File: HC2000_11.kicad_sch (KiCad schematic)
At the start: 16 parts

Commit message: Updated ICs values and positions
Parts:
- UA8, UC8: value 2k x 4bit -> 2k x 4bit/-
- UE8A0: value 27128P -> 27128P/-
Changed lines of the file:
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@@
       (effects (font (size 1.778 1.5113)) (justify left bottom))
     )
-    (property "Value" "2k x 4bit" (at 148.59 177.8 0)
+    (property "Value" "2k x 4bit/-" (at 148.59 177.8 0)
       (effects (font (size 1.778 1.5113)) (justify left bottom))
     )
@@
       (effects (font (size 1.778 1.5113)) (justify left bottom))
     )
-    (property "Value" "27128P" (at 107.95 167.64 0)
+    (property "Value" "27128P/-" (at 107.95 167.64 0)
       (effects (font (size 1.778 1.5113)) (justify left bottom))
     )
@@
       (effects (font (size 1.778 1.5113)) (justify left bottom))
     )
-    (property "Value" "2k x 4bit" (at 189.23 177.8 0)
-      (effects (font (size 1.778 1.5113)) (justify left bottom))
-    )
+    (property "Value" "2k x 4bit/-" (at 189.23 177.8 0)
+      (effects (font (size 1.778 1.5113)) (justify left bottom))
+    )

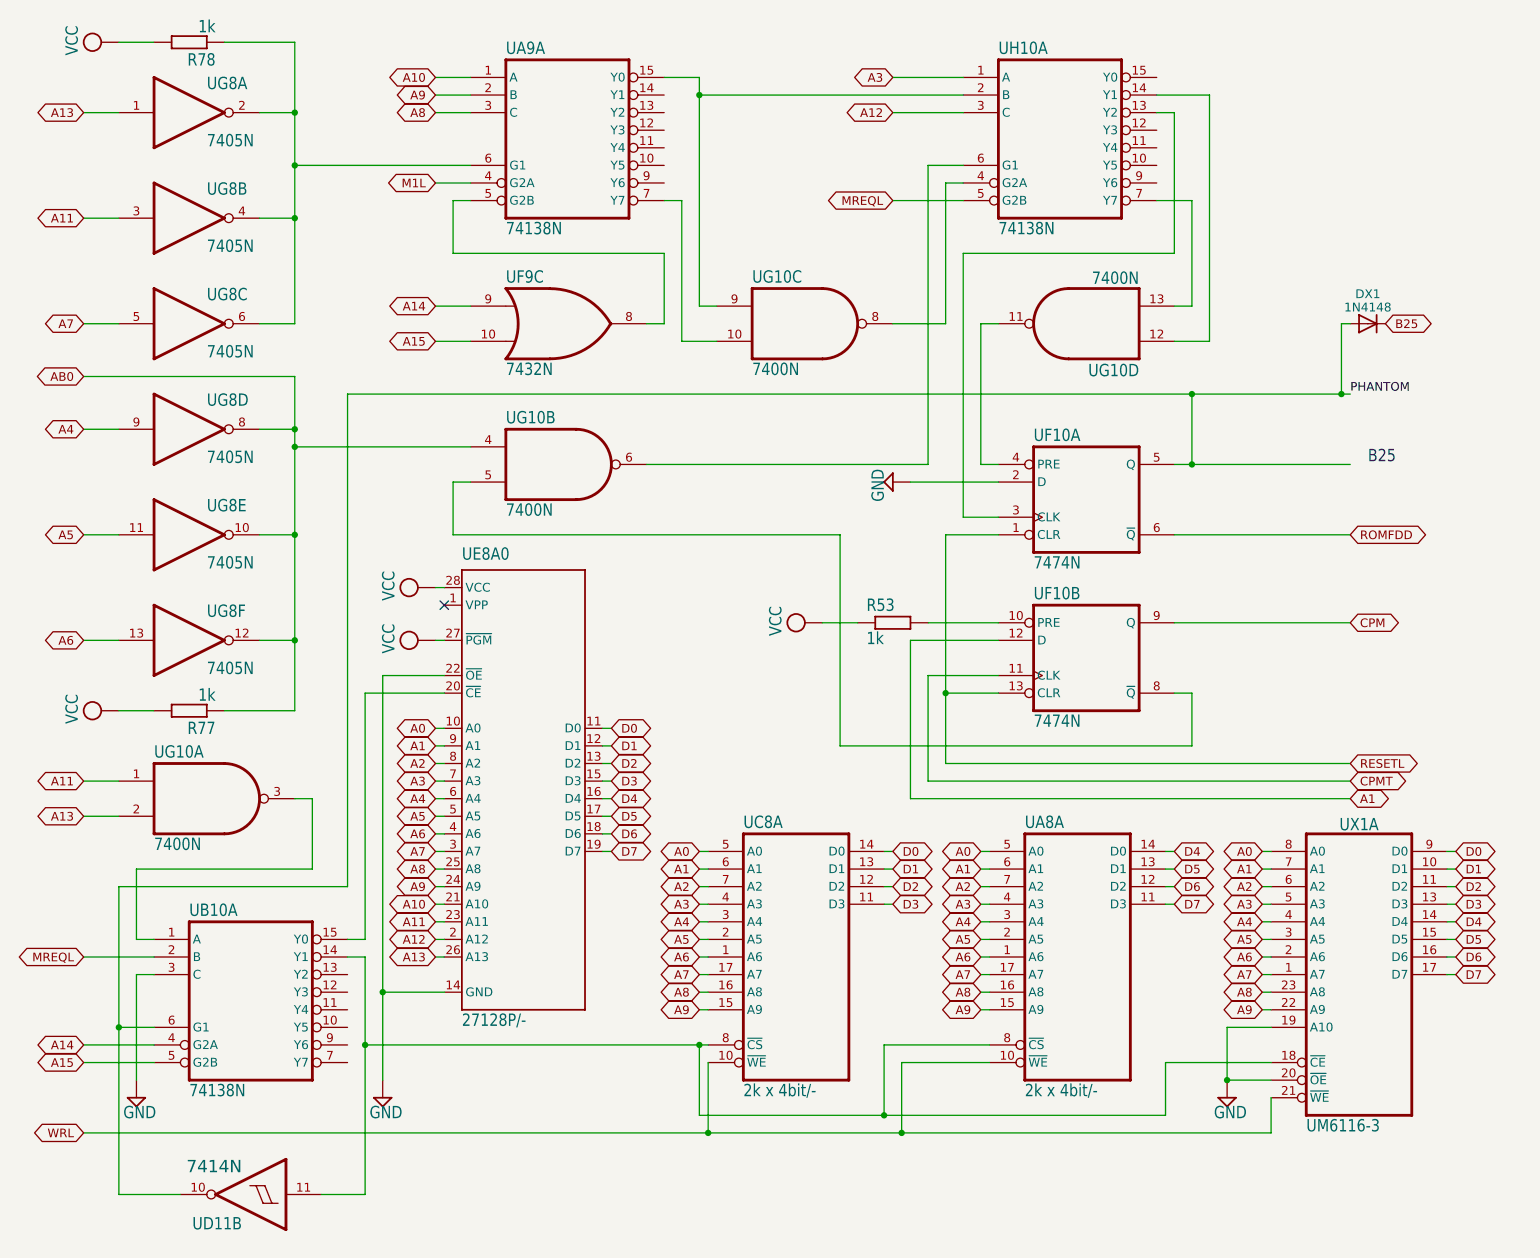
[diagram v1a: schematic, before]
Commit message: Fix errors (IC & unnoticed cut for 1 EPROM)
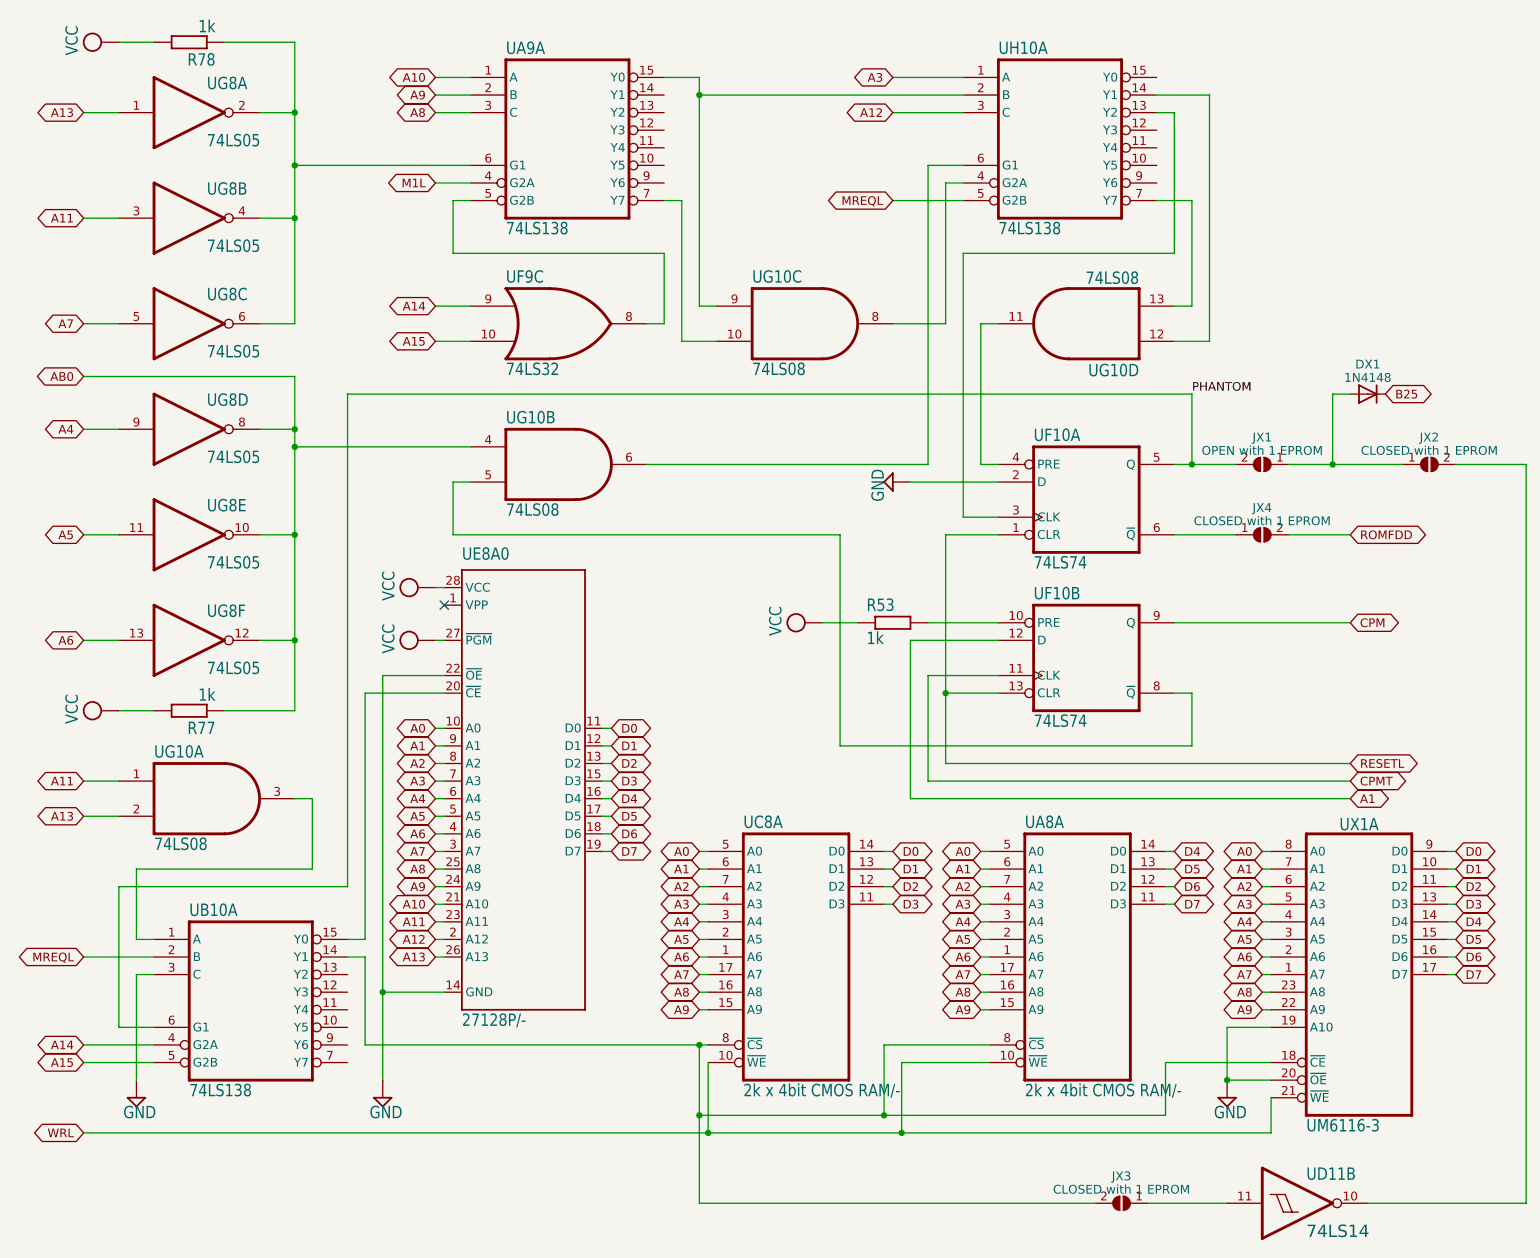
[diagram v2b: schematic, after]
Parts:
- added JX1: OPEN with 1 EPROM, HC2000:SolderJumper-2_P1.3mm_Open_Pad1.0x1.5mm, symbol HC2000:SolderJumper_2_Open
- added JX2, JX3, JX4: CLOSED with 1 EPROM, HC2000:SolderJumper-2_P1.3mm_Open_Pad1.0x1.5mm, symbol HC2000:SolderJumper_2_Open
- UA8, UC8: value 2k x 4bit/- -> 2k x 4bit CMOS RAM/-
- UA9, UB10, UH10: value 74138N -> 74LS138
- UD11: value 7414N -> 74LS14
- UF10: value 7474N -> 74LS74
- UF9: value 7432N -> 74LS32
- UG10: value 7400N -> 74LS08; symbol HC2000:7400N -> HC2000:7408N
- UG8: value 7405N -> 74LS05
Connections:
- net PHANTOM: now also JX1.2 (B); no longer DX1.A, UD11.10 (O)
- net ROMFDD: now also JX4.2 (B); no longer UF10.6 (~{Q})
- net at UA8.8 (~{CS}), UB10.14 (Y1), UC8.8 (~{CS})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: now also JX3.2 (B); no longer UD11.11 (I)
- new net: JX4.1 (A), UF10.6 (~{Q})
- new net: DX1.A, JX1.1 (A), JX2.1 (A)
- new net: JX2.2 (B), UD11.10 (O)
- new net: JX3.1 (A), UD11.11 (I)
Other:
- note removed: "B25"
- moved on the sheet: DX1, UD11B

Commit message: Revision-E
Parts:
- UA8, UC8: value 2k x 4bit CMOS RAM/- -> -
- UE8A0: value 27128P/- -> -
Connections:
- net ROMFDD: now also JX4.1 (A), UF10.6 (~{Q})
- net at JX3.2 (B), UA8.8 (~{CS}), UB10.14 (Y1)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: now also JX3.1 (A), UD11.11 (I)
- net at DX1.A, JX1.1 (A), JX2.1 (A): now also JX2.2 (B), UD11.10 (O)
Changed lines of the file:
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@@
 (kicad_sch (version 20230121) (generator eeschema)
   (paper "A4")
+  (junction (at 208.28 193.04) (diameter 0) (color 0 0 0 0)
+  )
   (junction (at 83.82 81.28) (diameter 0) (color 0 0 0 0)
   )
@@
   (junction (at 218.44 175.26) (diameter 0) (color 0 0 0 0)
   )
+  (junction (at 198.12 193.04) (diameter 0) (color 0 0 0 0)
+  )
   (junction (at 142.24 33.02) (diameter 0) (color 0 0 0 0)
   )
@@
   (junction (at 83.82 35.56) (diameter 0) (color 0 0 0 0)
   )
+  (junction (at 242.57 86.36) (diameter 0) (color 0 0 0 0)
+  )
   (junction (at 171.45 182.88) (diameter 0) (color 0 0 0 0)
   )
@@
   (junction (at 96.52 162.56) (diameter 0) (color 0 0 0 0)
   )
+  (junction (at 228.6 96.52) (diameter 0) (color 0 0 0 0)
+  )
+  (junction (at 218.44 96.52) (diameter 0) (color 0 0 0 0)
+  )
   (junction (at 142.24 170.18) (diameter 0) (color 0 0 0 0)
+  )
+  (junction (at 252.73 86.36) (diameter 0) (color 0 0 0 0)
   )
   (junction (at 177.8 119.38) (diameter 0) (color 0 0 0 0)
@@
     (stroke (width 0) (type default))
   )
+  (wire (pts (xy 218.44 99.06) (xy 228.6 99.06))
+    (stroke (width 0) (type default))
+  )
+  (wire (pts (xy 198.12 195.58) (xy 208.28 195.58))
+    (stroke (width 0) (type default))
+  )
   (wire (pts (xy 106.68 96.52) (xy 106.68 88.9))
     (stroke (width 0) (type default))
@@
     (stroke (width 0) (type default))
   )
+  (wire (pts (xy 208.28 193.04) (xy 218.44 193.04))
+    (stroke (width 0) (type default))
+  )
   (wire (pts (xy 251.46 144.78) (xy 250.19 144.78))
     (stroke (width 0) (type default))
@@
     (stroke (width 0) (type default))
   )
-  (wire (pts (xy 251.46 86.36) (xy 261.62 86.36))
+  (wire (pts (xy 251.46 86.36) (xy 252.73 86.36))
     (stroke (width 0) (type default))
   )
@@
     (stroke (width 0) (type default))
   )
+  (wire (pts (xy 228.6 96.52) (xy 227.33 96.52))
+    (stroke (width 0) (type default))
+  )
   (wire (pts (xy 91.44 147.32) (xy 58.42 147.32))
     (stroke (width 0) (type default))
@@
     (stroke (width 0) (type default))
   )
+  (wire (pts (xy 218.44 96.52) (xy 210.82 96.52))
+    (stroke (width 0) (type default))
+  )
+  (wire (pts (xy 242.57 86.36) (xy 243.84 86.36))
+    (stroke (width 0) (type default))
+  )
   (wire (pts (xy 251.46 147.32) (xy 250.19 147.32))
     (stroke (width 0) (type default))
@@
     (stroke (width 0) (type default))
   )
-  (wire (pts (xy 207.01 193.04) (xy 218.44 193.04))
+  (wire (pts (xy 207.01 193.04) (xy 208.28 193.04))
     (stroke (width 0) (type default))
   )
@@
     (stroke (width 0) (type default))
   )
-  (wire (pts (xy 219.71 96.52) (xy 210.82 96.52))
+  (wire (pts (xy 219.71 96.52) (xy 218.44 96.52))
     (stroke (width 0) (type default))
   )
@@
     (stroke (width 0) (type default))
   )
+  (wire (pts (xy 252.73 88.9) (xy 252.73 86.36))
+    (stroke (width 0) (type default))
+  )
+  (wire (pts (xy 252.73 86.36) (xy 261.62 86.36))
+    (stroke (width 0) (type default))
+  )
   (wire (pts (xy 177.8 119.38) (xy 185.42 119.38))
     (stroke (width 0) (type default))
@@
     (stroke (width 0) (type default))
   )
+  (wire (pts (xy 242.57 88.9) (xy 252.73 88.9))
+    (stroke (width 0) (type default))
+  )
   (wire (pts (xy 213.36 127) (xy 162.56 127))
     (stroke (width 0) (type default))
@@
     (stroke (width 0) (type default))
   )
+  (wire (pts (xy 228.6 99.06) (xy 228.6 96.52))
+    (stroke (width 0) (type default))
+  )
   (wire (pts (xy 170.18 35.56) (xy 180.34 35.56))
     (stroke (width 0) (type default))
@@
     (stroke (width 0) (type default))
   )
-  (wire (pts (xy 233.68 86.36) (xy 243.84 86.36))
+  (wire (pts (xy 233.68 86.36) (xy 242.57 86.36))
     (stroke (width 0) (type default))
   )
@@
     (stroke (width 0) (type default))
   )
+  (wire (pts (xy 218.44 96.52) (xy 218.44 99.06))
+    (stroke (width 0) (type default))
+  )
   (wire (pts (xy 170.18 147.32) (xy 168.91 147.32))
     (stroke (width 0) (type default))
@@
     (stroke (width 0) (type default))
   )
+  (wire (pts (xy 198.12 193.04) (xy 198.12 195.58))
+    (stroke (width 0) (type default))
+  )
   (wire (pts (xy 233.68 86.36) (xy 233.68 76.2))
     (stroke (width 0) (type default))
@@
     (stroke (width 0) (type default))
   )
-  (wire (pts (xy 142.24 193.04) (xy 199.39 193.04))
+  (wire (pts (xy 142.24 193.04) (xy 198.12 193.04))
     (stroke (width 0) (type default))
   )
@@
     (stroke (width 0) (type default))
   )
+  (wire (pts (xy 198.12 193.04) (xy 199.39 193.04))
+    (stroke (width 0) (type default))
+  )
   (wire (pts (xy 53.34 66.04) (xy 58.42 66.04))
     (stroke (width 0) (type default))
@@
     (stroke (width 0) (type default))
   )
+  (wire (pts (xy 208.28 195.58) (xy 208.28 193.04))
+    (stroke (width 0) (type default))
+  )
   (wire (pts (xy 142.24 162.56) (xy 143.51 162.56))
     (stroke (width 0) (type default))
@@
     (stroke (width 0) (type default))
   )
-  (wire (pts (xy 236.22 96.52) (xy 227.33 96.52))
+  (wire (pts (xy 236.22 96.52) (xy 228.6 96.52))
     (stroke (width 0) (type default))
   )
@@
   )
   (wire (pts (xy 215.9 33.02) (xy 208.28 33.02))
+    (stroke (width 0) (type default))
+  )
+  (wire (pts (xy 242.57 86.36) (xy 242.57 88.9))
     (stroke (width 0) (type default))
   )
@@
       (effects (font (size 1.778 1.5113)) (justify left bottom))
     )
-    (property "Value" "2k x 4bit CMOS RAM/-" (at 148.59 177.8 0)
+    (property "Value" "-" (at 148.59 177.8 0)
       (effects (font (size 1.778 1.5113)) (justify left bottom))
     )
@@
       (effects (font (size 1.778 1.5113)) (justify left bottom))
     )
-    (property "Value" "27128P/-" (at 107.95 167.64 0)
+    (property "Value" "-" (at 107.95 167.64 0)
       (effects (font (size 1.778 1.5113)) (justify left bottom))
     )
@@
       (effects (font (size 1.778 1.5113)) (justify left bottom))
     )
-    (property "Value" "2k x 4bit CMOS RAM/-" (at 189.23 177.8 0)
-      (effects (font (size 1.778 1.5113)) (justify left bottom))
-    )
+    (property "Value" "-" (at 189.23 177.8 0)
+      (effects (font (size 1.778 1.5113)) (justify left bottom))
+    )
